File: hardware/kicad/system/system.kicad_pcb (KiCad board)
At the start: 2 copper layers, 200 x 130 mm, 131 parts, among them M501 IRF530, Q201 IRF540N, Q202 IRF530, Q401 IRF530, SW201 Switch, U201 LM7805, U202 MCP601, U203 NE555, U204 ILD74, U205 MCP601, U206 IR2110, U207 4N25, U208 IR2110, U301 MCP601, U302 IL300, U303 MCP601, U401 CNY17, U402 IR2110, U501 CNY17, U502 IR2110

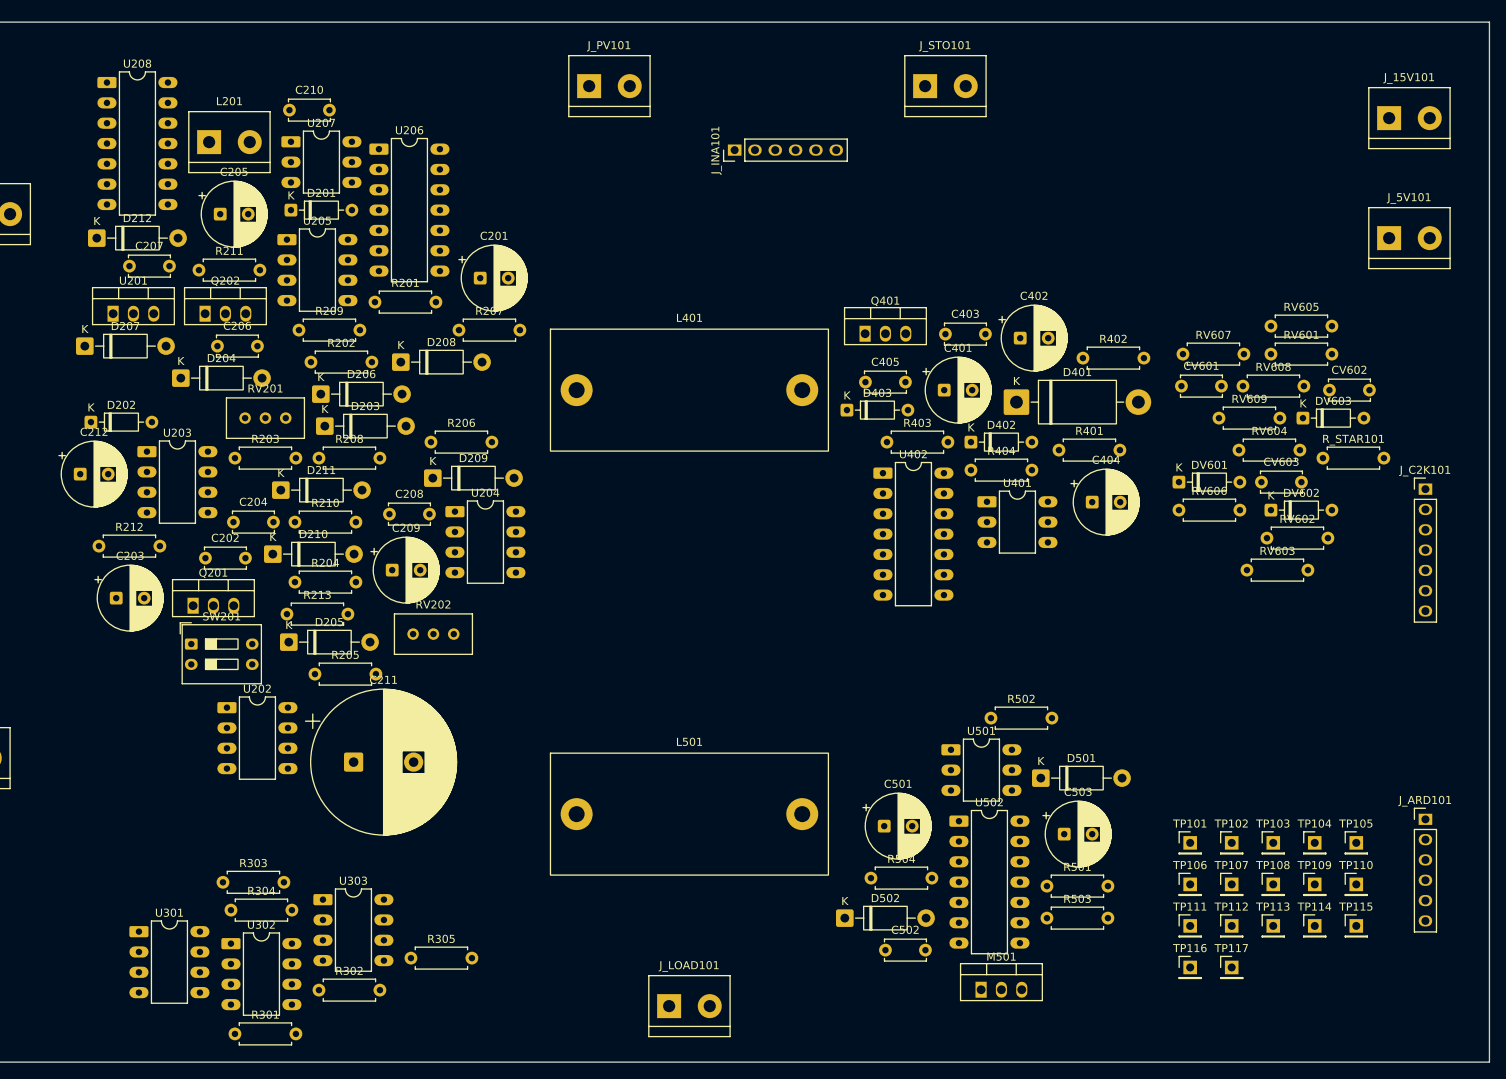
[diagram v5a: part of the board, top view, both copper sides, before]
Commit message: system PCB: grid-aligned, justified re-placement (spacious, 0 overlaps)
Replace the cramped force-directed layout. place_system3.py packs each functional
block into neat justified rows (even spacing -> routing channels), groups same-type
parts, lays tall parts (DIPs/TO-220) on their side for short uniform rows, snaps to
a 1 mm grid. Regions sized ~proportional to part-need; mppt & boost placed SIDE BY
SIDE in the centre (each full height) so neither overflows. Connectors on the edges.
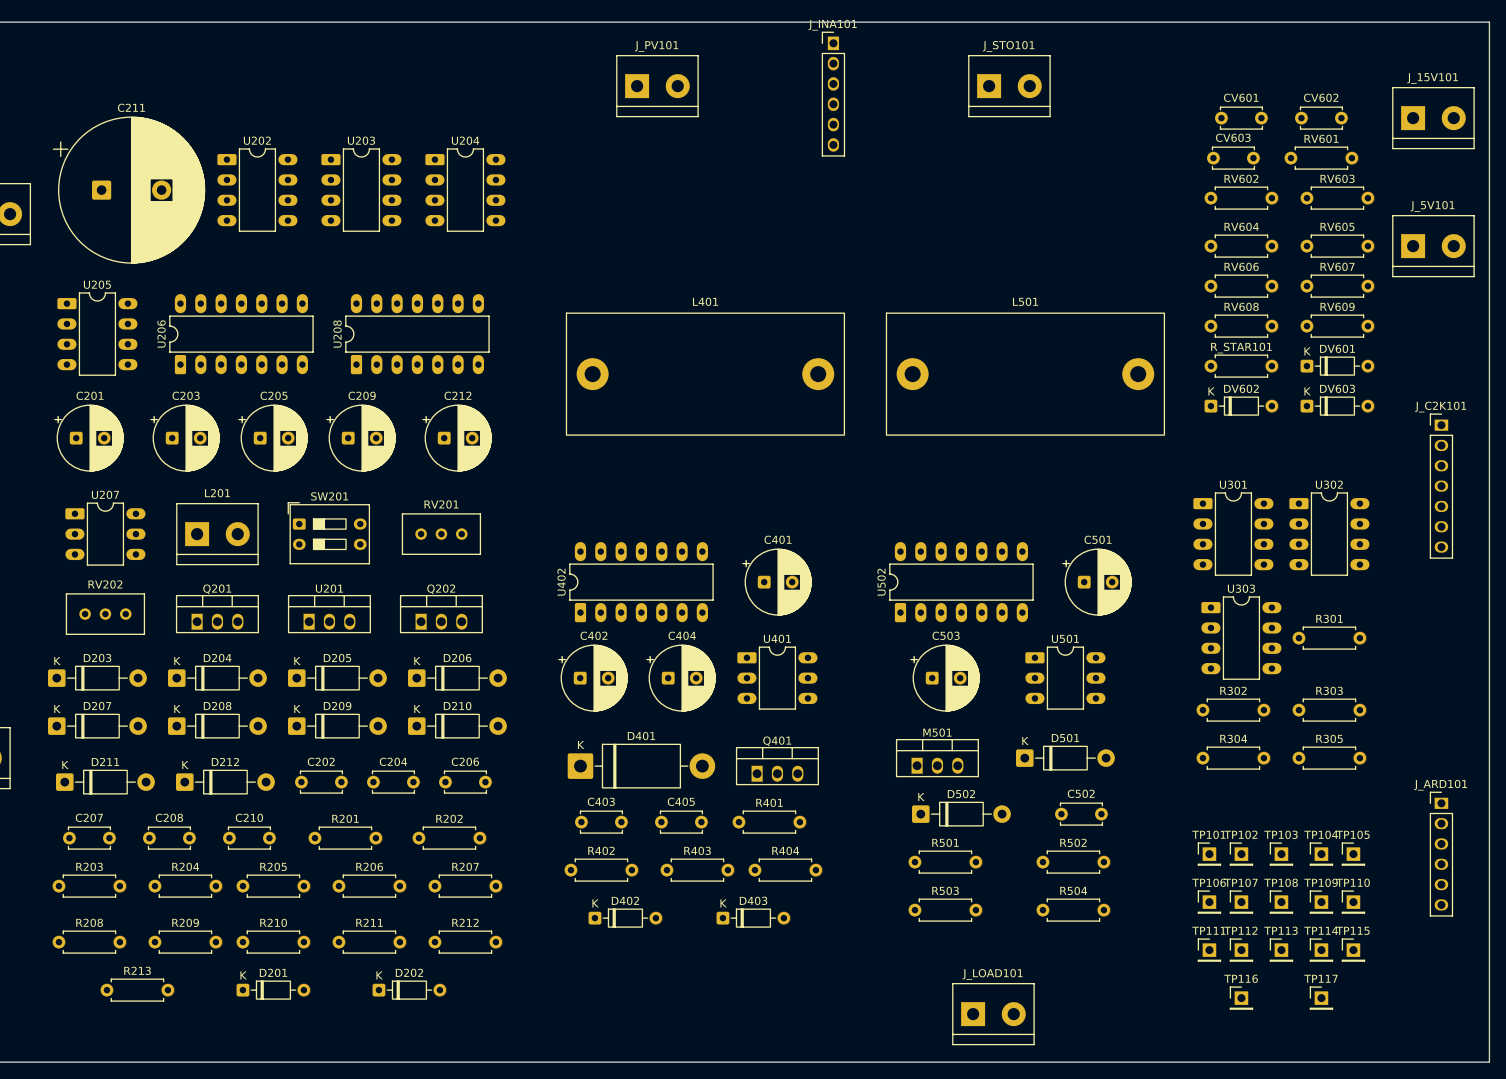
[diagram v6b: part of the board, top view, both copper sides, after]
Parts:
- moved U302 144.4 mm to (176.2, 60.2)
- moved U301 143.4 mm to (164.2, 60.2)
- moved R301 141.9 mm to (176.2, 77.0)
- moved R303 136.2 mm to (176.2, 86.0)
- moved R304 123.0 mm to (164.2, 92.0)
- moved U303 116.8 mm to (165.2, 73.2)
- moved R302 115.9 mm to (164.2, 86.0)
- moved R305 113.8 mm to (176.2, 92.0)
- moved D201 97.7 mm to (44.2, 121.0)
- moved C210 91.3 mm to (42.5, 102.0)
- moved R402 90.5 mm to (85.2, 106.0)
- moved R211 85.8 mm to (56.2, 115.0)
- moved D202 79.6 mm to (61.2, 121.0)
- moved R209 78.6 mm to (33.2, 115.0)
- moved C211 78.1 mm to (26.5, 21.0)
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
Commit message: system PCB: placement CSV round-trip tool + current placed board
- placement_csv.py: export/apply the placement through a human-editable CSV
  (ref,value,footprint,x,y,rotation,side) so alignment/spacing can be tuned in a
  spreadsheet and applied back -- the kicad-parts-placer idea without the dependency
- system_placement.csv: current grid-aligned placement (131 parts)
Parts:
- moved C212 114.2 mm to (166.5, 112.0)
- moved C401 114.2 mm to (206.5, 130.0)
- moved C402 114.2 mm to (183.5, 142.0)
- moved C404 114.2 mm to (194.5, 142.0)
- moved D204 114.2 mm to (133.1, 142.0)
- moved D205 114.2 mm to (148.1, 142.0)
- moved D206 114.2 mm to (163.1, 142.0)
- moved D208 114.2 mm to (133.1, 148.0)
- moved D209 114.2 mm to (148.1, 148.0)
- moved D210 114.2 mm to (163.1, 148.0)
- moved D212 114.2 mm to (134.1, 155.0)
- moved D501 114.2 mm to (239.1, 152.0)
- moved D502 114.2 mm to (226.1, 159.0)
- moved J_MOT101 114.2 mm to (104.7, 152.0)
- moved J_PV101 114.2 mm to (190.7, 68.0)
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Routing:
- added copper zone on B.Cu, net GND
- added copper zone on F.Cu, net GND

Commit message: system PCB: restore grid-aligned placement (working copy was clobbered by an open KiCad autosave)
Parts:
- moved C212 114.2 mm to (69.3, 52.0)
- moved C401 114.2 mm to (109.3, 70.0)
- moved C402 114.2 mm to (86.3, 82.0)
- moved C404 114.2 mm to (97.3, 82.0)
- moved D204 114.2 mm to (35.9, 82.0)
- moved D205 114.2 mm to (50.9, 82.0)
- moved D206 114.2 mm to (65.9, 82.0)
- moved D208 114.2 mm to (35.9, 88.0)
- moved D209 114.2 mm to (50.9, 88.0)
- moved D210 114.2 mm to (65.9, 88.0)
- moved D212 114.2 mm to (36.9, 95.0)
- moved D501 114.2 mm to (141.9, 92.0)
- moved D502 114.2 mm to (128.9, 99.0)
- moved J_MOT101 114.2 mm to (7.46, 92.0)
- moved J_PV101 114.2 mm to (93.5, 8.00)
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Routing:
- removed copper zone on B.Cu, net GND
- removed copper zone on F.Cu, net GND
